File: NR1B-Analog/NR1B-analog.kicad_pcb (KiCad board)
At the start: 4 copper layers, 71.1 x 134.5 mm, 82 parts, among them J1 Conn_02x04_Odd_Even, J2 Conn_02x04_Odd_Even, J3 Conn_01x03_Male, J8 Conn_01x04_Male, SW1 1-1571636-0, U1 DAC11001BPFBR, U10 LT3042MPMSE-PBF, U11 LDK320ADU120R, U12 20K, U13 OPA2189IDR, U14 DAC11001BPFBR, U2 ADR444ARZ, U3 OPA189IDGKT, U4 OPA2189IDR, U5 Pico, U7 LT3093EMSE-PBF, U8 20K, U9 10K, X1 NUCLEO144-ZIO

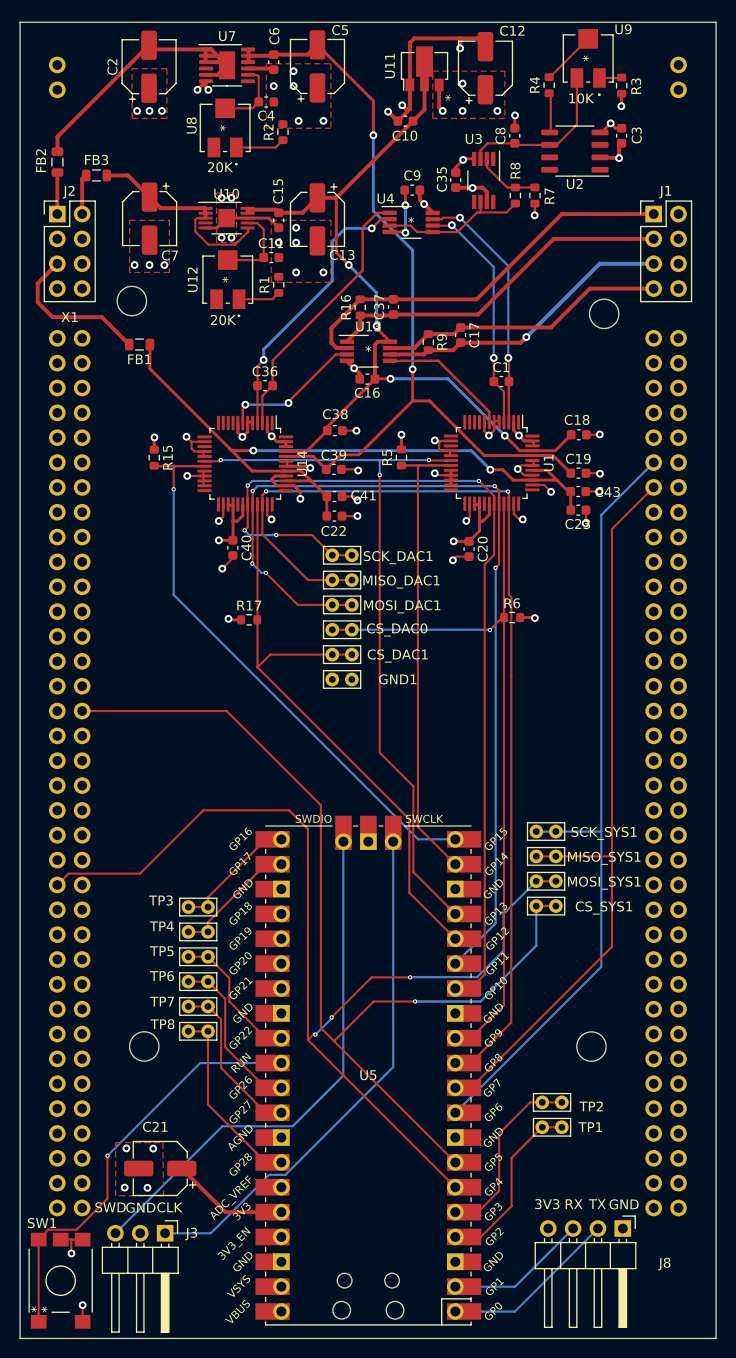
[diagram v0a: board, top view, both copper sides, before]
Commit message: Added ADC for voltage reading
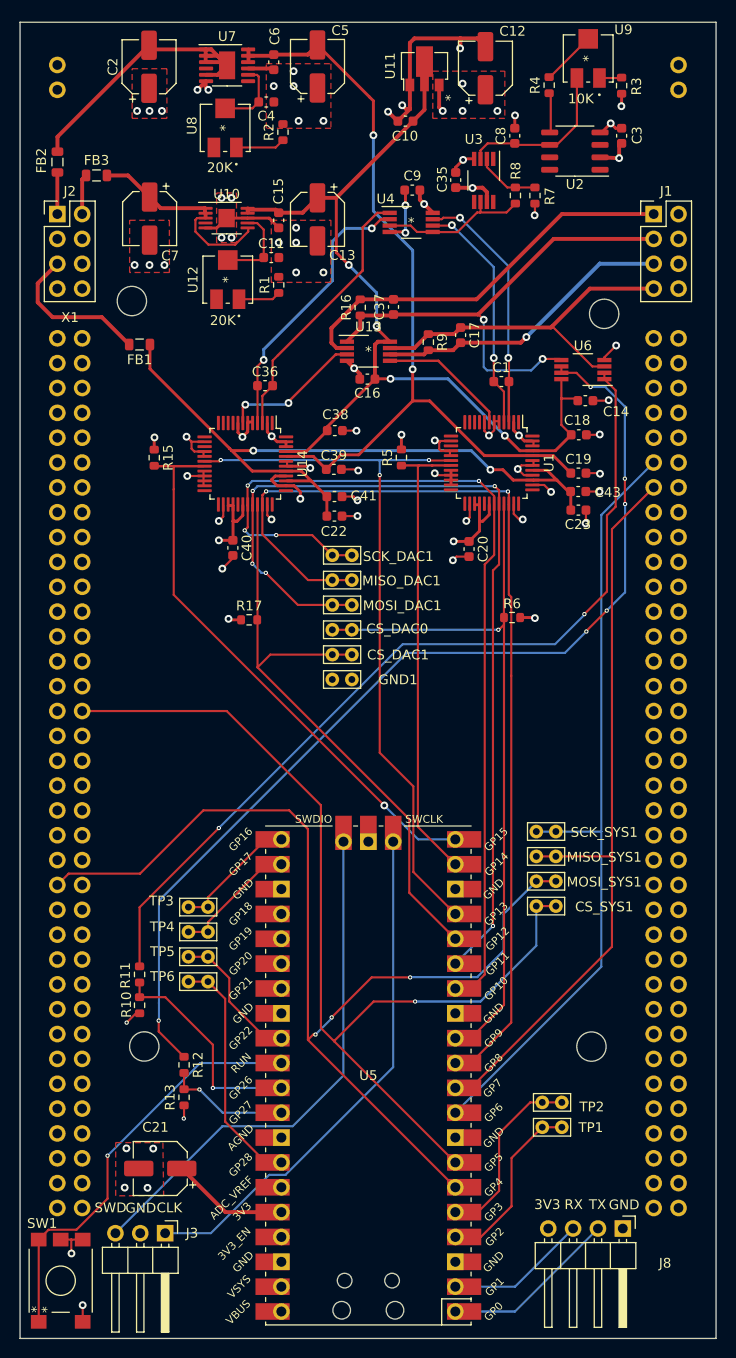
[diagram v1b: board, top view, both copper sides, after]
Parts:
- removed TP7, TP8: TestPoint, TestPoint:TestPoint_Bridge_Pitch2.0mm_Drill0.7mm
- added C14: 0.1uF, Capacitor_SMD:C_0603_1608Metric, F.Cu at (106.8, 57.3)
- added R10: 50K, Resistor_SMD:R_0603_1608Metric, F.Cu at (61.2, 119.1)
- added R11: 100K, Resistor_SMD:R_0603_1608Metric, F.Cu at (61.2, 116.0)
- added R12: 100K, Resistor_SMD:R_0603_1608Metric, F.Cu at (65.8, 125.2)
- added R13: 50K, Resistor_SMD:R_0603_1608Metric, F.Cu at (65.8, 128.5)
- added U6: OPA2189IDR, Package_SO:VSSOP-8_3.0x3.0mm_P0.65mm, F.Cu at (106.5, 54.1)
- U1, U14: footprint Package_QFP:LQFP-48_7x7mm_P0.5mm -> Package_QFP:TQFP-48_7x7mm_P0.5mm
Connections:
- TP6 pad 1: Net-(TP6-Pad1) -> Net-(U5-Pad34)
- U5 pad 31: Net-(TP6-Pad1) -> /MCU/DAC0_READ
- U5 pad 32: Net-(TP7-Pad1) -> /MCU/DAC1_READ
- U5 pad 34: Net-(TP8-Pad1) -> Net-(U5-Pad34)
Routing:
- net Net-(U6-Pad6): track 0.00 -> 105.4 mm, vias 0 -> 6
- net Net-(U6-Pad1): track 0.00 -> 90.4 mm, vias 0 -> 2
- net Net-(U5-Pad34): track 0.00 -> 24.5 mm
- net /MCU/DAC0_READ: track 0.00 -> 22.4 mm, vias 0 -> 1
- net Net-(TP8-Pad1): track 19.4 -> 0.00 mm
- net Net-(TP7-Pad1): track 16.9 -> 0.00 mm
- net Net-(TP6-Pad1): track 16.9 -> 0.00 mm
- net OUT_DRIVE1: track 36.5 -> 50.7 mm, vias 0 -> 2
- net /MCU/DAC1_READ: track 0.00 -> 12.6 mm, vias 0 -> 1
- net +14Vreg: track 83.4 -> 91.3 mm
- net OUT_DRIVE0: track 29.4 -> 36.5 mm
- net GND: track 124.8 -> 131.5 mm, vias 65 -> 69

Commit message: Fixed symbol libs, see notes from July 25 on PCB and schema
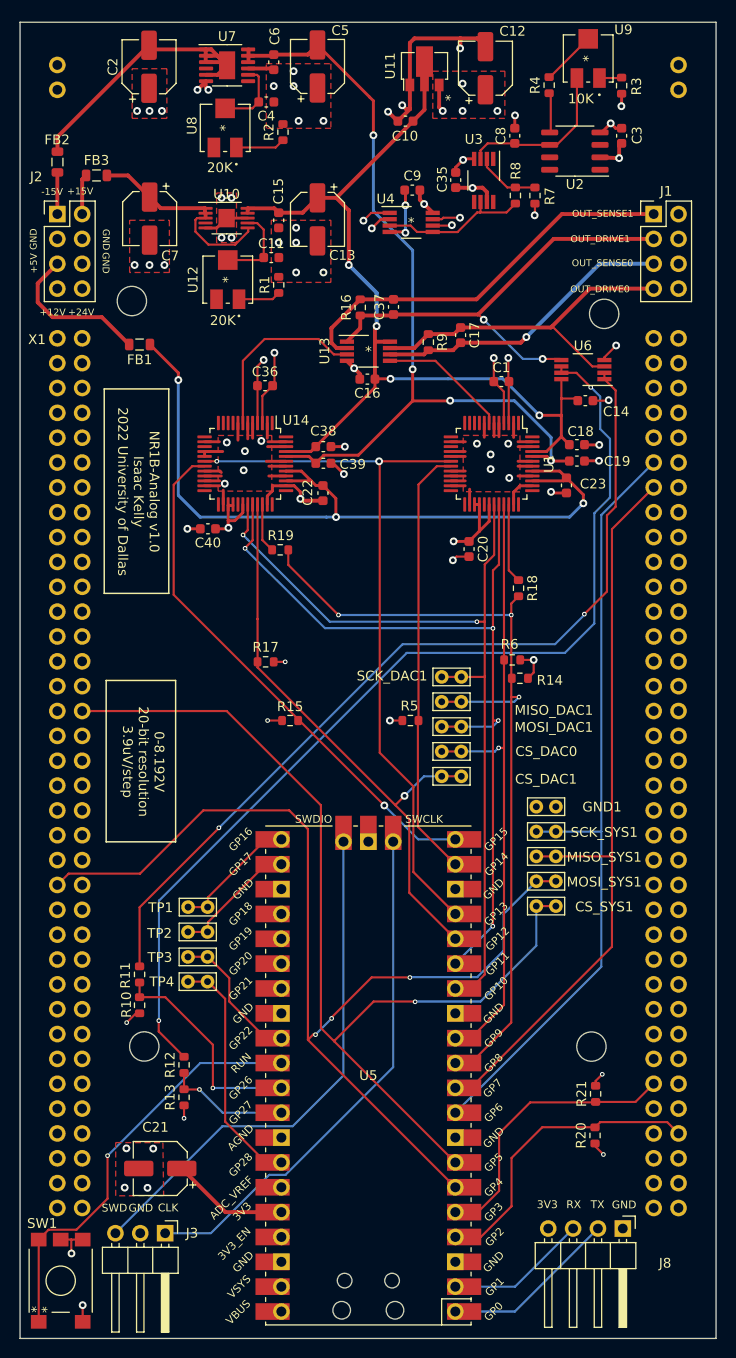
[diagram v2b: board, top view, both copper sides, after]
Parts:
- removed C41, C43: 0.1uF, Capacitor_SMD:C_0603_1608Metric
- removed TP5, TP6: TestPoint, TestPoint:TestPoint_Bridge_Pitch2.0mm_Drill0.7mm
- added R14: 10K, Resistor_SMD:R_0603_1608Metric, F.Cu at (100.1, 85.7)
- added R18: 47, Resistor_SMD:R_0603_1608Metric, F.Cu at (100.0, 76.5)
- added R19: 47, Resistor_SMD:R_0603_1608Metric, F.Cu at (75.6, 72.5)
- added R20: 10K, Resistor_SMD:R_0603_1608Metric, F.Cu at (107.8, 132.4)
- added R21: 10K, Resistor_SMD:R_0603_1608Metric, F.Cu at (107.8, 128.2)
- J3: value Conn_01x03_Male -> SWD
- J8: value Conn_01x04_Male -> UART
- R10, R13: value 50K -> 47K
- moved TP1 42.6 mm to (66.2, 109.1)
- moved TP2 40.2 mm to (66.2, 111.6)
- moved R15 30.2 mm to (76.6, 90.0), turned to 0 degrees
- moved R5 26.9 mm to (88.9, 90.0), turned to 180 degrees
- moved GND1 24.6 mm to (101.8, 98.8)
- moved CS_DAC0 16.7 mm to (92.1, 93.2)
- moved CS_DAC1 16.7 mm to (92.1, 95.7)
- moved MISO_DAC1 16.7 mm to (92.1, 88.1)
- moved MOSI_DAC1 16.7 mm to (92.1, 90.6)
- moved SCK_DAC1 16.7 mm to (92.1, 85.5)
- moved TP3 5.09 mm to (66.2, 114.2)
- moved TP4 5.08 mm to (66.2, 116.7)
- moved R17 4.61 mm to (74.1, 84.0), turned to 180 degrees
- moved R6 4.33 mm to (99.3, 83.8)
- moved C40 3.21 mm to (68.2, 70.4), turned to 180 degrees
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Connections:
- J1 pad 8: /Interconnect/ANA_CE -> unconnected-(J1-Pad8)
- R12 pad 1: Net-(U6-Pad6) -> /MCU/DAC1_READ
- R12 pad 2: /MCU/DAC1_READ -> Net-(U6-Pad6)
- TP1 pad 1: Net-(TP1-Pad1) -> Net-(U5-Pad21)
- TP4 pad 1: Net-(TP4-Pad1) -> Net-(U5-Pad34)
- U1 pad 34: /MCU/MISO_DAC -> Net-(U1-Pad34)
- U14 pad 34: /MCU/MISO_DAC -> Net-(U14-Pad34)
- U5 pad 21: Net-(TP3-Pad1) -> Net-(U5-Pad21)
- U5 pad 22: Net-(TP4-Pad1) -> Net-(TP2-Pad1)
- U5 pad 29: Net-(TP5-Pad1) -> Net-(TP3-Pad1)
- U5 pad 4: Net-(TP1-Pad1) -> /Interconnect/ACK
- U5 pad 5: Net-(TP2-Pad1) -> /Interconnect/ERROR
- X1 pad 133: unconnected-(X1-Pad133) -> /Interconnect/ERROR
- X1 pad 138: unconnected-(X1-Pad138) -> /Interconnect/ACK
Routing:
- net /Interconnect/ACK: track 0.00 -> 31.1 mm
- net /Interconnect/ERROR: track 0.00 -> 29.1 mm
- net Net-(TP1-Pad1): track 18.4 -> 0.00 mm
- net /MCU/MISO_DAC: track 102.2 -> 86.7 mm, vias 2 -> 3
- net Net-(TP5-Pad1): track 14.4 -> 0.00 mm
- net Net-(TP4-Pad1): track 13.0 -> 0.00 mm
- net Net-(U5-Pad21): track 0.00 -> 13.0 mm
- net /MCU/CS_DAC0: track 76.0 -> 64.0 mm
- net +5V: track 71.5 -> 81.0 mm, vias 2 -> 3
- net Net-(U1-Pad34): track 0.00 -> 8.15 mm
- net /MCU/SCK_DAC: track 95.6 -> 88.1 mm, vias 4 -> 2
- net /MCU/MOSI_DAC: track 95.2 -> 89.0 mm, vias 5 -> 4
- net Net-(TP2-Pad1): track 19.0 -> 13.0 mm
- net Net-(U14-Pad34): track 0.00 -> 5.05 mm
- net +3V3: track 43.4 -> 47.8 mm, vias 6 -> 8
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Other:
- board text added: "+12V"
- board text added: "+15V"
- board text added: "+24V"
- board text added: "+5V"
- board text added: "-15V"
- board text added: "0-8.192V 20-bit resolution 3.9uV/step"
- board text added: "NR1B-Analog v1.0 Isaac Kelly 2022 University of Dallas"
- board text added: "OUT_DRIVE0"
- board text added: "OUT_DRIVE1"
- board text added: "OUT_SENSE0"
- board text added: "OUT_SENSE1"

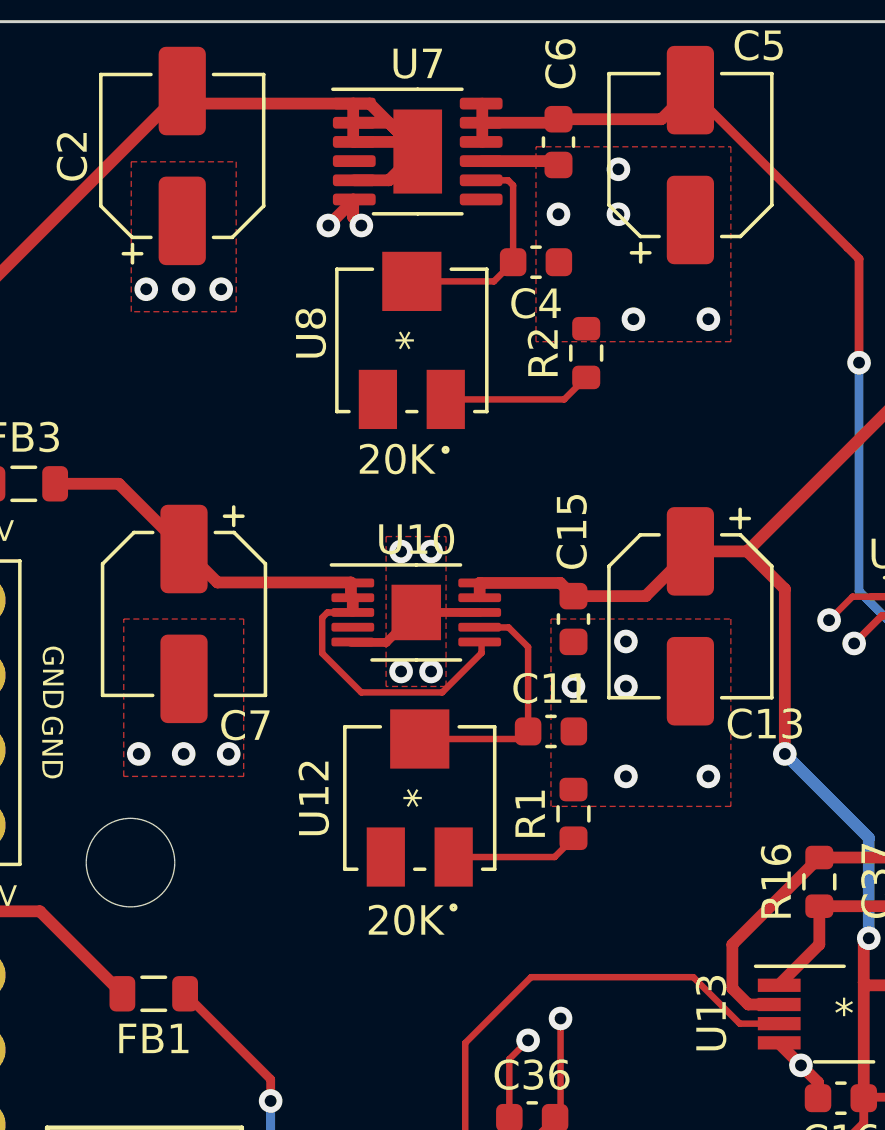
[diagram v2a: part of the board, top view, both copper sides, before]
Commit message: Labeled sheets, adjusted pot location
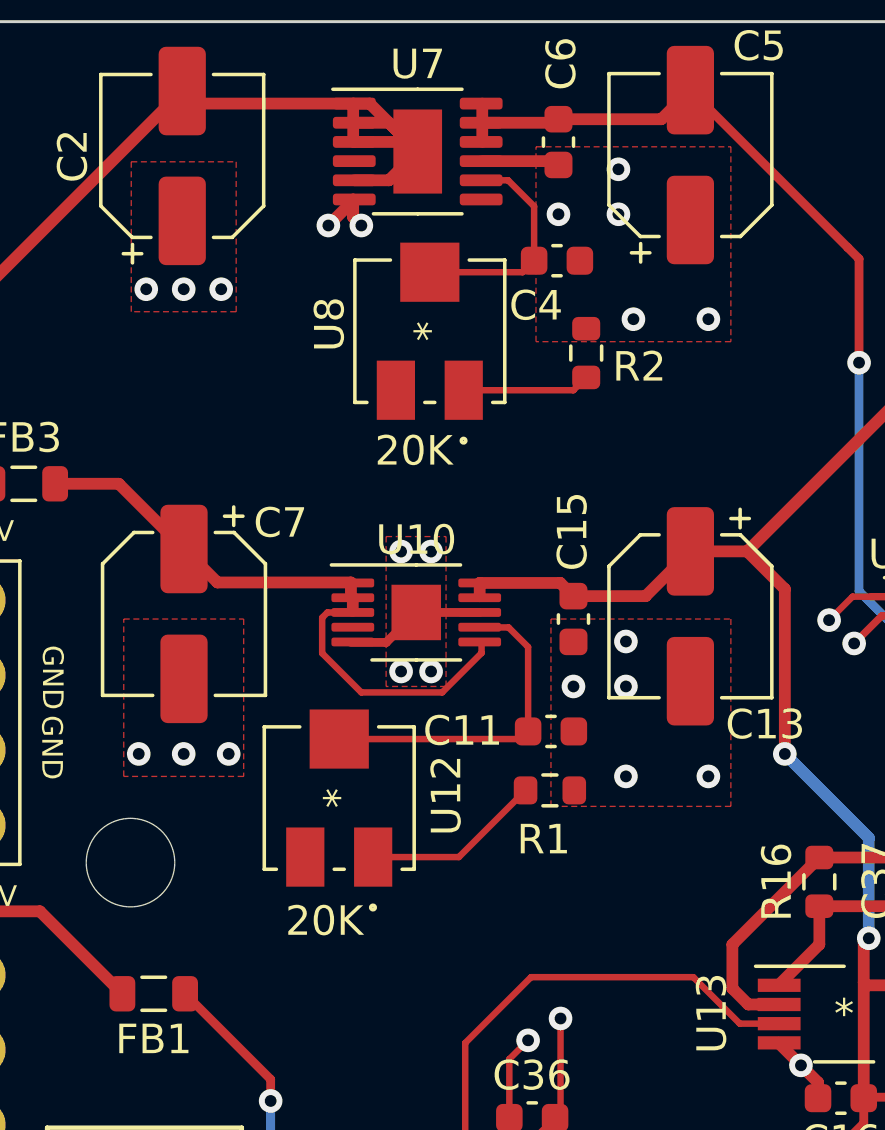
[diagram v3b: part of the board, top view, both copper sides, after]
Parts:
- moved U12 2.73 mm to (67.5, 44.9)
- moved R1 1.13 mm to (74.6, 44.7), turned to 0 degrees
- moved C4 0.71 mm to (74.9, 26.7)
- moved U8 0.68 mm to (70.6, 29.1)
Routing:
- net Net-(C11-Pad1): track 8.49 -> 11.2 mm
- net Net-(R1-Pad1): track 4.32 -> 6.10 mm
- net Net-(R2-Pad1): track 5.07 -> 4.33 mm

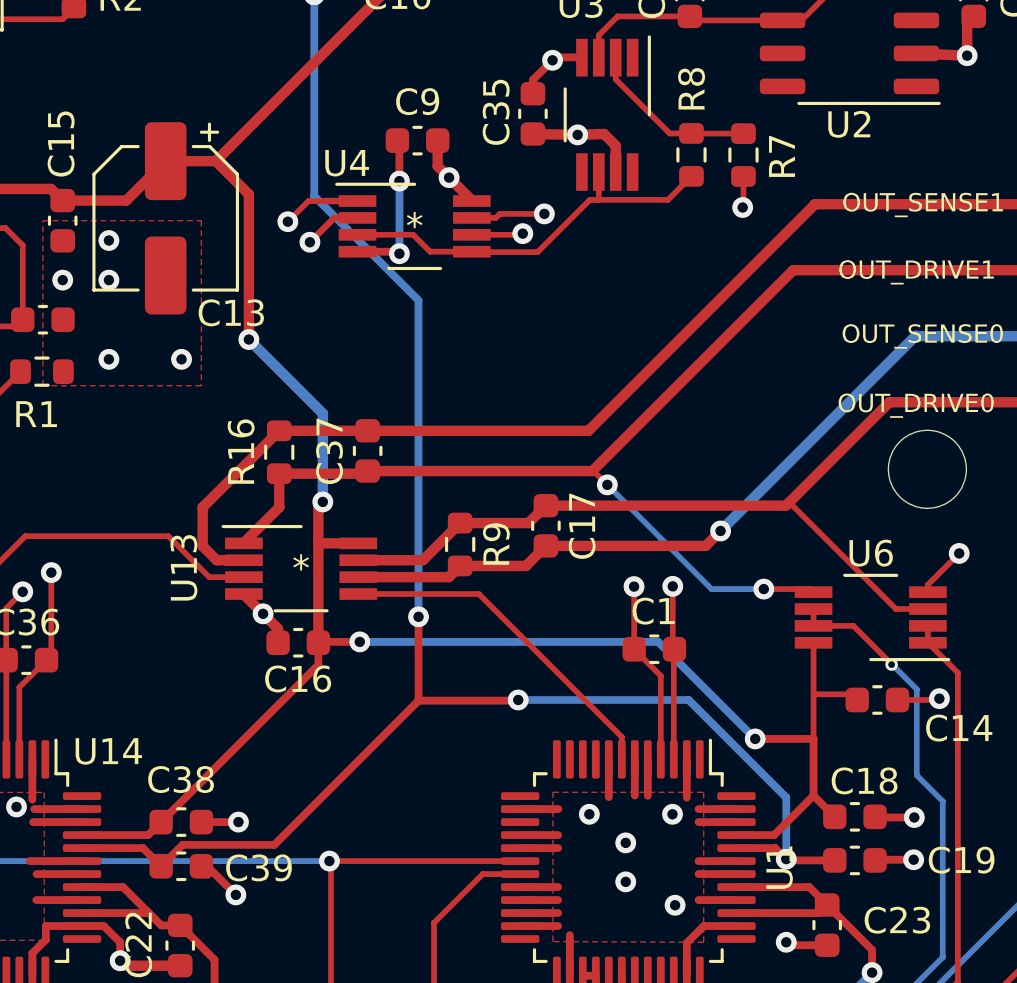
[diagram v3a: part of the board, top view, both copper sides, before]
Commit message: 12v supply to dual op-amps
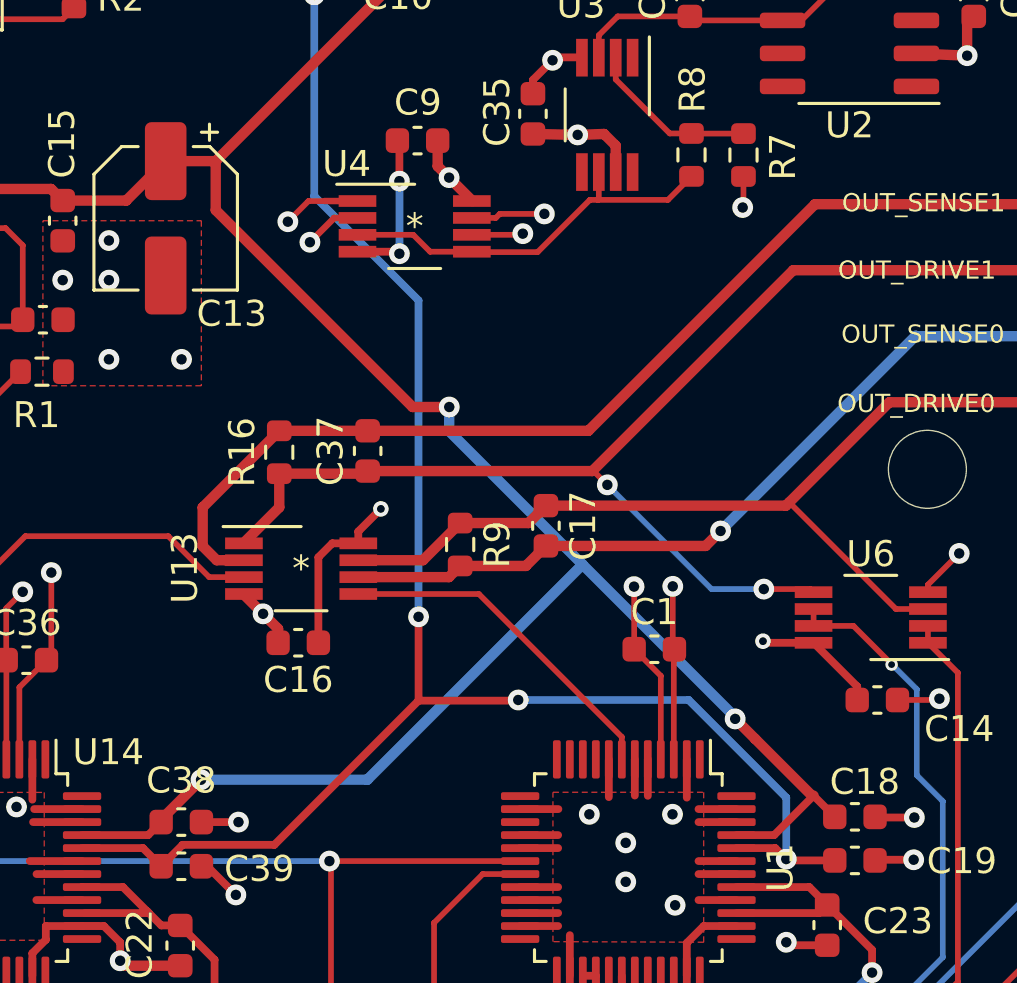
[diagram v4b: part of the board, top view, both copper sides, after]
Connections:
- C14 pad 1: +14Vreg -> +12Vref
- C16 pad 1: +14Vreg -> +12Vref
- U13 pad 8: +14Vreg -> +12Vref
- U6 pad 8: +14Vreg -> +12Vref
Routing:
- net +12Vref: track 13.4 -> 25.0 mm, vias 7 -> 9
- net +14Vreg: track 93.0 -> 88.4 mm, vias 4 -> 3
